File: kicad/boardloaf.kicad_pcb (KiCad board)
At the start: 2 copper layers, 100 x 100 mm, 41 parts, among them J1 AudioJack4, J2 AudioJack4, SW1 SW_Push, SW10 SW_Push, SW11 SW_Push, SW12 SW_Push, SW13 SW_Push, SW14 SW_Push, SW15 SW_Push, SW16 SW_Push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

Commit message: align hole
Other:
- outline, holes or cut-outs redrawn
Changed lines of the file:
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@@
 	)
 	(gr_circle
-		(center 86 112.5)
-		(end 84 112.5)
+		(center 85.5 112.5)
+		(end 83.5 112.5)
 		(stroke
 			(width 0.05)
@@
 	)
 	(via
-		(at 86 109.5)
+		(at 85.5 109.5)
 		(size 0.6)
 		(drill 0.3)
@@
 	)
 	(via
-		(at 86 116.25)
+		(at 85.5 116.25)
 		(size 0.6)
 		(drill 0.3)

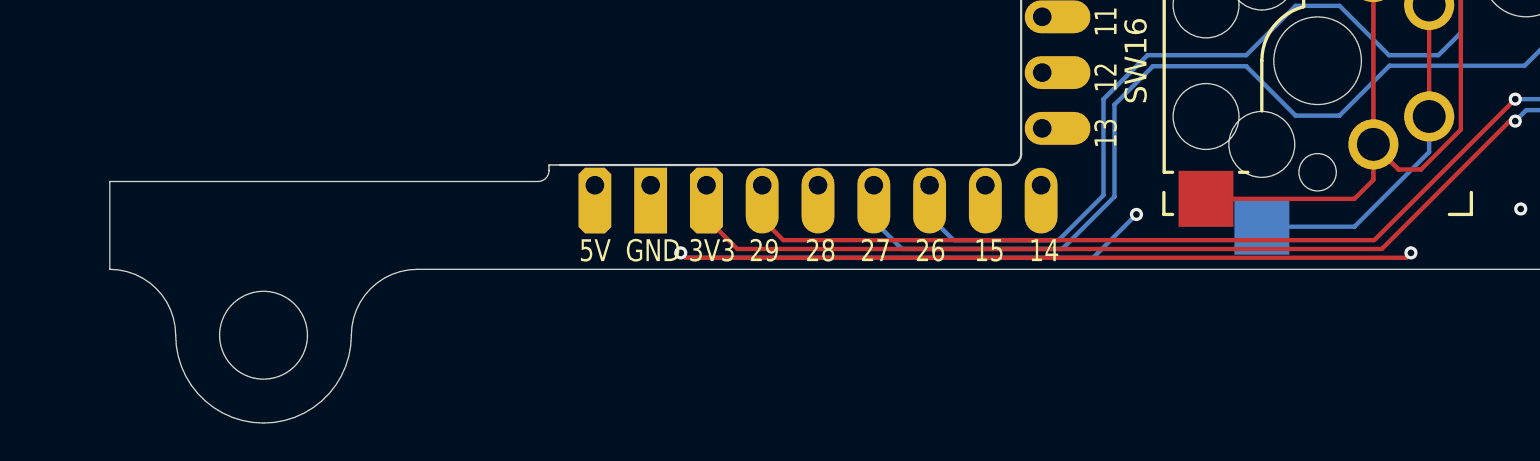
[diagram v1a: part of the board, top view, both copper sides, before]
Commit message: fix schema and add jumper
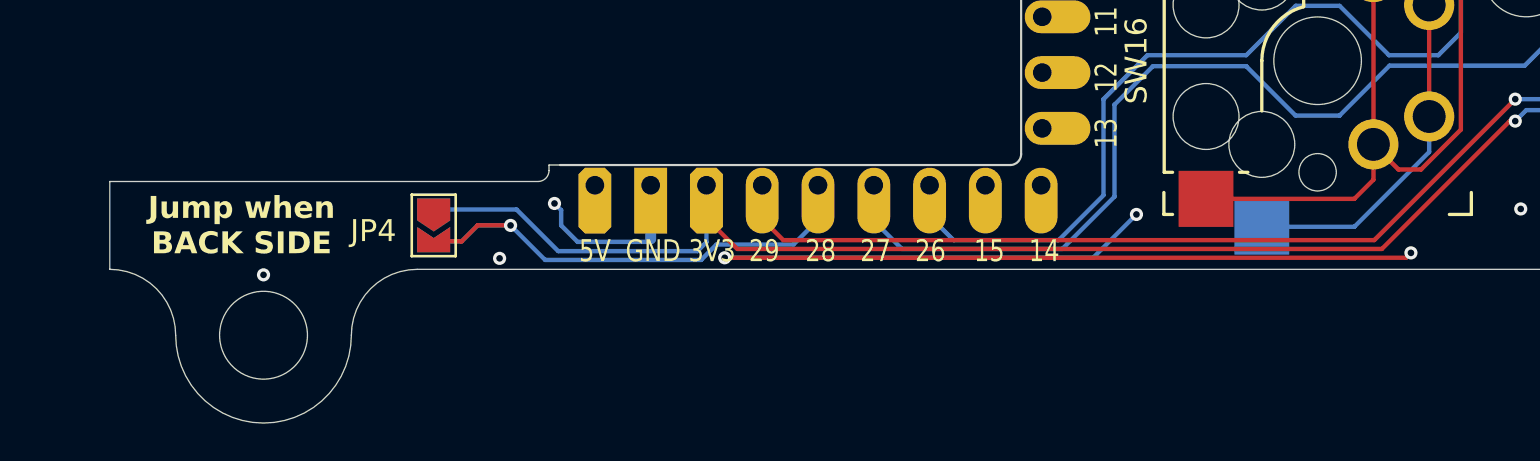
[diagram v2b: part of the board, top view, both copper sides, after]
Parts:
- added JP3: SolderJumper_2_Open, Jumper:SolderJumper-2_P1.3mm_Open_TrianglePad1.0x1.5mm, B.Cu at (82.2, 134.5)
- added JP4: SolderJumper_2_Open, Jumper:SolderJumper-2_P1.3mm_Open_TrianglePad1.0x1.5mm, F.Cu at (82.2, 134.5)
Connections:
- U1 pad 28: unconnected-(U1-Pad28) -> Net-(JP3-B)
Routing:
- net Net-(JP3-B): track 0.00 -> 24.6 mm, vias 0 -> 1
- net VCC: track 79.5 -> 96.6 mm
- net GND: track 55.1 -> 58.9 mm, vias 19 -> 22

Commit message: update gubber
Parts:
- moved JP3 1.00 mm to (81.2, 134.5)
- moved JP4 1.00 mm to (81.2, 134.5)
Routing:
- net Net-(JP3-B): track 24.6 -> 26.6 mm
- net GND: track 58.9 -> 57.9 mm
- net VCC: track 96.6 -> 97.6 mm
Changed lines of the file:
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@@
 	(footprint "Jumper:SolderJumper-2_P1.3mm_Open_TrianglePad1.0x1.5mm"
 		(layer "F.Cu")
-		(at 82.25 134.5 -90)
+		(at 81.25 134.5 -90)
 		(descr "SMD Solder Jumper, 1x1.5mm Triangular Pads, 0.3mm gap, open")
 		(tags "solder jumper open")
 		(property "Reference" "JP4"
-			(at 0.25 2.75 180)
+			(at 0 -2.75 180)
 			(layer "F.SilkS")
 			(effects
@@
 	(footprint "Jumper:SolderJumper-2_P1.3mm_Open_TrianglePad1.0x1.5mm"
 		(layer "B.Cu")
-		(at 82.25 134.5 -90)
+		(at 81.25 134.5 -90)
 		(descr "SMD Solder Jumper, 1x1.5mm Triangular Pads, 0.3mm gap, open")
 		(tags "solder jumper open")
 		(property "Reference" "JP3"
-			(at 0.25 2.75 0)
+			(at 0 -2.75 0)
 			(layer "B.SilkS")
 			(effects
@@
 	)
 	(gr_text "Jump when\nBACK SIDE"
-		(at 73.5 134.5 0)
+		(at 75.5 134.5 0)
 		(layer "F.SilkS")
 		(effects
@@
 	)
 	(gr_text "Jump when\nBACK SIDE"
-		(at 73.5 134.5 -0)
+		(at 75.5 134.5 -0)
 		(layer "B.SilkS")
 		(effects
@@
 	)
 	(via
-		(at 85.25 136)
+		(at 85.75 136)
 		(size 0.6)
 		(drill 0.3)
@@
 	)
 	(via
-		(at 87.75 133.5)
+		(at 88 134.5)
 		(size 0.6)
 		(drill 0.3)
@@
 	)
 	(segment
-		(start 88.802 135.25)
+		(start 89 135.25)
 		(end 92 135.25)
 		(width 0.2)
@@
 	)
 	(segment
-		(start 88.052 133.802)
-		(end 88.052 134.5)
-		(width 0.2)
+		(start 92.13 135.12)
+		(end 92.13 132.67)
+		(width 0.5)
 		(layer "B.Cu")
 		(net 23)
 	)
 	(segment
-		(start 92 135.25)
-		(end 92.13 135.12)
+		(start 88.25 134.5)
+		(end 89 135.25)
 		(width 0.2)
 		(layer "B.Cu")
@@
 	)
 	(segment
-		(start 88.052 134.5)
-		(end 88.802 135.25)
+		(start 92 135.25)
+		(end 92.13 135.12)
 		(width 0.2)
 		(layer "B.Cu")
@@
 	)
 	(segment
-		(start 92.13 135.12)
-		(end 92.13 132.67)
-		(width 0.5)
+		(start 88 134.5)
+		(end 88.25 134.5)
+		(width 0.2)
 		(layer "B.Cu")
 		(net 23)
@@
 	)
 	(segment
-		(start 87.75 133.5)
-		(end 88.052 133.802)
-		(width 0.2)
-		(layer "B.Cu")
-		(net 23)
-	)
-	(segment
 		(start 150.5 123.775)
 		(end 150.5 120.25)
@@
 	)
 	(segment
+		(start 87.921 135.671)
+		(end 86.025 133.775)
+		(width 0.2)
+		(layer "B.Cu")
+		(net 31)
+	)
+	(segment
 		(start 140.500001 131.491146)
 		(end 142.508854 131.491146)
@@
 	)
 	(segment
-		(start 94.67 135.2629)
-		(end 94.2619 135.671)
-		(width 0.2)
-		(layer "B.Cu")
-		(net 31)
-	)
-	(segment
 		(start 132 129.25)
 		(end 138.258855 129.25)
@@
 	)
 	(segment
-		(start 144.75 129.25)
-		(end 148.753 129.25)
+		(start 94.67 135.2629)
+		(end 94.2619 135.671)
 		(width 0.2)
 		(layer "B.Cu")
@@
 	)
 	(segment
-		(start 138.258855 129.25)
-		(end 140.500001 131.491146)
+		(start 94.2619 135.671)
+		(end 87.921 135.671)
 		(width 0.2)
 		(layer "B.Cu")
@@
 	)
 	(segment
-		(start 86.025 133.775)
-		(end 82.25 133.775)
+		(start 144.75 129.25)
+		(end 148.753 129.25)
 		(width 0.2)
 		(layer "B.Cu")
@@
 	)
 	(segment
-		(start 94.2619 135.671)
-		(end 87.921 135.671)
+		(start 94.67 132.67)
+		(end 94.67 135.2629)
 		(width 0.2)
 		(layer "B.Cu")
@@
 	)
 	(segment
-		(start 87.921 135.671)
-		(end 86.025 133.775)
+		(start 138.258855 129.25)
+		(end 140.500001 131.491146)
 		(width 0.2)
 		(layer "B.Cu")
@@
 	)
 	(segment
-		(start 131.5 129.75)
-		(end 132 129.25)
+		(start 86.025 133.775)
+		(end 81.25 133.775)
 		(width 0.2)
 		(layer "B.Cu")
@@
 	)
 	(segment
-		(start 94.67 132.67)
-		(end 94.67 135.2629)
+		(start 131.5 129.75)
+		(end 132 129.25)
 		(width 0.2)
 		(layer "B.Cu")
@@
 	)
 	(segment
-		(start 83.525 135.225)
-		(end 82.25 135.225)
+		(start 84.25 134.5)
+		(end 83.525 135.225)
 		(width 0.2)
 		(layer "F.Cu")
@@
 	)
 	(segment
-		(start 84.25 134.5)
-		(end 83.525 135.225)
+		(start 83.525 135.225)
+		(end 81.25 135.225)
 		(width 0.2)
 		(layer "F.Cu")
@@
 	)
 	(segment
-		(start 85.75 134.5)
-		(end 84.25 134.5)
-		(width 0.2)
-		(layer "B.Cu")
-		(net 36)
-	)
-	(segment
 		(start 84.25 134.5)
 		(end 83.525 135.225)
@@
 	)
 	(segment
+		(start 85.75 134.5)
+		(end 84.25 134.5)
+		(width 0.2)
+		(layer "B.Cu")
+		(net 36)
+	)
+	(segment
 		(start 99.75 134.25)
 		(end 98.628 135.372)
@@
 	(segment
 		(start 83.525 135.225)
-		(end 82.25 135.225)
+		(end 81.25 135.225)
 		(width 0.2)
 		(layer "B.Cu")
